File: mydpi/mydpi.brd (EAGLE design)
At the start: 41 x 20 mm, 36 parts, among them Q1 DMN3404L, U1 MEGA32U4-MU, U2 RT9193-33GB, Y1 830069392

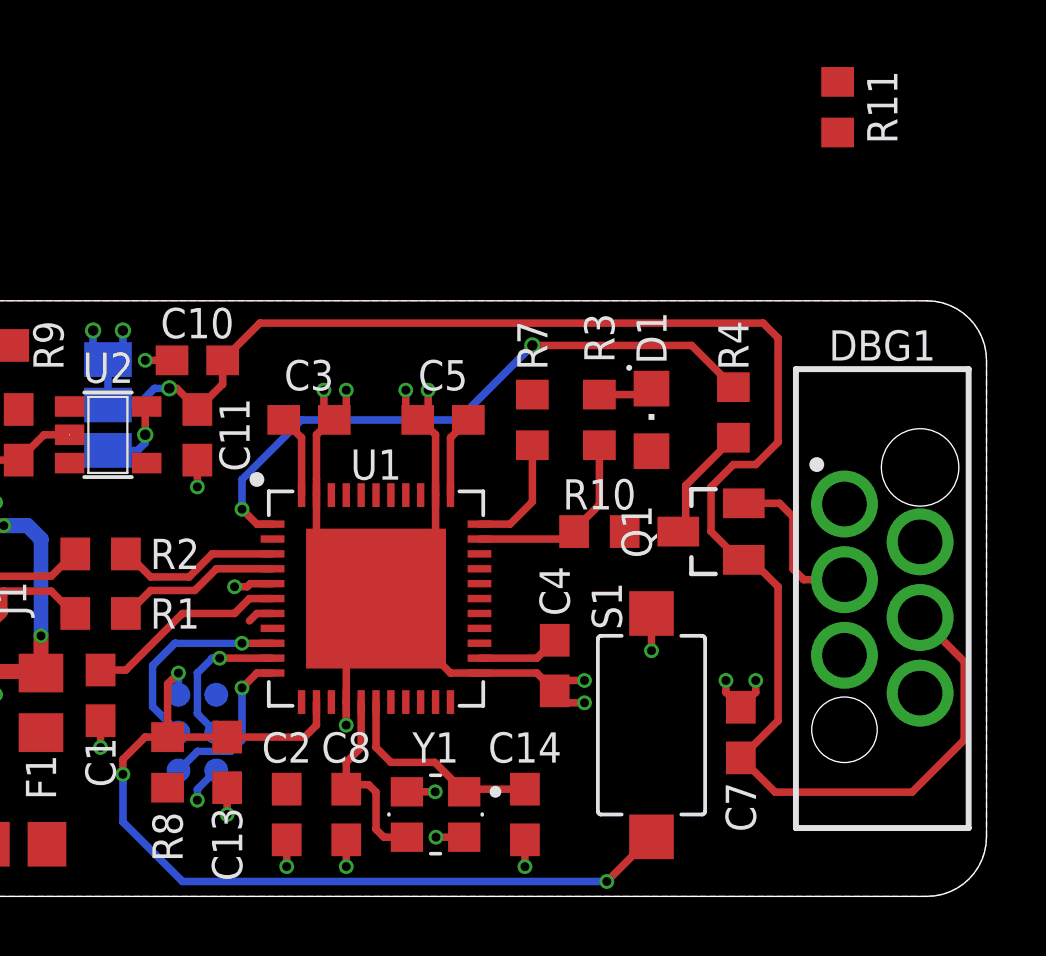
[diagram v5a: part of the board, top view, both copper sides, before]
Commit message: Routing Pullup Resistors
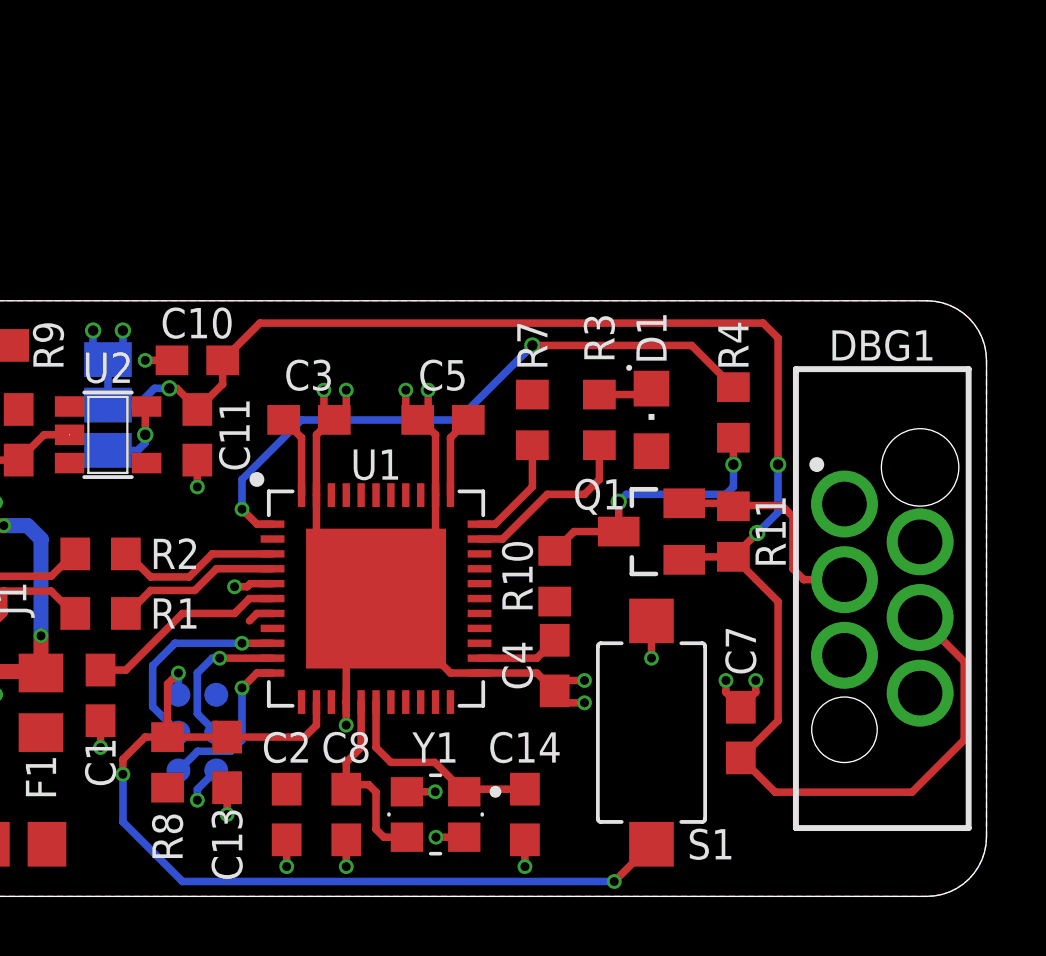
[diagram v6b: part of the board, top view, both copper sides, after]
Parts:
- moved R11 14.7 mm to (32.5, 12.2)
- moved R10 2.12 mm to (26.5, 10.8), turned to 270 degrees
- moved Q1 2.00 mm to (29.8, 12.2)
- moved S1 0.25 mm to (29.8, 5.50)
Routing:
- net UDPI_RAW: track 3.92 -> 9.13 mm, vias 0 -> 2
- net UDPI: track 5.47 -> 7.49 mm
- net VTG: track 57.0 -> 57.4 mm, vias 1 -> 3
